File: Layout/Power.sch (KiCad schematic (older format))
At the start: 0 parts

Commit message: Add voltage regulators
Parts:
- added C? (x2): 10u, symbol Device:C
- added C?: 1u, symbol Device:C
- added C? (x4): 0.1u, symbol Device:C
- added C? (x2): 22u, symbol Device:C
- added D? (x4): US1M, Diode_SMD:D_SMA, symbol Diode:US1M
- added L?: 2.2u, symbol Device:L
- added R?: 49.9k, symbol Device:R_US
- added R?: 9.09k, symbol Device:R_US
- added R?: 1k, symbol Device:R_US
- added U?: TPS562200, Package_TO_SOT_SMD:SOT-23-6, symbol Regulator_Switching:TPS562200
- added U?: AP2112K-3.3, Package_TO_SOT_SMD:SOT-23-5, symbol Regulator_Linear:AP2112K-3.3
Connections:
- new net: C?.1, L?.1, U?.2 (SW)
- new net: R?.1, R?.1, U?.4 (VFB)
- new net: R?.1, U?.5 (EN)
- new net: C?.2, U?.6 (VBST)
- new net +3V3: C?.1, U?.5 (VOUT)
- new net +5V: C?.1, C?.1, C?.1, L?.2, R?.2, U?.1 (VIN), U?.3 (EN)
- new net +VDC: C?.1, C?.1, C?.1, C?.1, D?.1 (K), D?.1 (K), R?.2, U?.3 (VIN)
- new net GND: C?.2, C?.2, C?.2, C?.2, C?.2, C?.2, C?.2, C?.2, D?.2 (A), D?.2 (A), R?.2, U?.1 (GND), U?.2 (GND)
- new net PRI_HI: D?.1 (K), D?.2 (A)
- new net PRI_LO: D?.1 (K), D?.2 (A)

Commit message: Add footprints
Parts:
- C? (x9): footprint (none) -> Capacitor_SMD:C_0603_1608Metric_Pad1.05x0.95mm_HandSolder
- L?: footprint (none) -> Inductor_SMD:L_0603_1608Metric_Pad1.05x0.95mm_HandSolder
- R? (x3): footprint (none) -> Resistor_SMD:R_0603_1608Metric_Pad1.05x0.95mm_HandSolder
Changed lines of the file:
@@
 F 0 "C?" H 4465 2146 50  0000 L CNN
 F 1 "10u" H 4465 2055 50  0000 L CNN
-F 2 "" H 4388 1950 50  0001 C CNN
+F 2 "Capacitor_SMD:C_0603_1608Metric_Pad1.05x0.95mm_HandSolder" H 4388 1950 50  0001 C CNN
 F 3 "~" H 4350 2100 50  0001 C CNN
 	1    4350 2100
@@
 F 0 "C?" H 4865 2146 50  0000 L CNN
 F 1 "10u" H 4865 2055 50  0000 L CNN
-F 2 "" H 4788 1950 50  0001 C CNN
+F 2 "Capacitor_SMD:C_0603_1608Metric_Pad1.05x0.95mm_HandSolder" H 4788 1950 50  0001 C CNN
 F 3 "~" H 4750 2100 50  0001 C CNN
 	1    4750 2100
@@
 F 0 "C?" H 5265 2146 50  0000 L CNN
 F 1 "1u" H 5265 2055 50  0000 L CNN
-F 2 "" H 5188 1950 50  0001 C CNN
+F 2 "Capacitor_SMD:C_0603_1608Metric_Pad1.05x0.95mm_HandSolder" H 5188 1950 50  0001 C CNN
 F 3 "~" H 5150 2100 50  0001 C CNN
 	1    5150 2100
@@
 F 0 "C?" H 5665 2146 50  0000 L CNN
 F 1 "0.1u" H 5665 2055 50  0000 L CNN
-F 2 "" H 5588 1950 50  0001 C CNN
+F 2 "Capacitor_SMD:C_0603_1608Metric_Pad1.05x0.95mm_HandSolder" H 5588 1950 50  0001 C CNN
 F 3 "~" H 5550 2100 50  0001 C CNN
 	1    5550 2100
@@
 F 0 "L?" V 3790 4350 50  0000 C CNN
 F 1 "2.2u" V 3699 4350 50  0000 C CNN
-F 2 "" H 3600 4350 50  0001 C CNN
+F 2 "Inductor_SMD:L_0603_1608Metric_Pad1.05x0.95mm_HandSolder" H 3600 4350 50  0001 C CNN
 F 3 "~" H 3600 4350 50  0001 C CNN
 	1    3600 4350
@@
 F 0 "C?" V 3802 4900 50  0000 C CNN
 F 1 "0.1u" V 3711 4900 50  0000 C CNN
-F 2 "" H 3588 4750 50  0001 C CNN
+F 2 "Capacitor_SMD:C_0603_1608Metric_Pad1.05x0.95mm_HandSolder" H 3588 4750 50  0001 C CNN
 F 3 "~" H 3550 4900 50  0001 C CNN
 	1    3550 4900
@@
 F 0 "C?" H 4065 4546 50  0000 L CNN
 F 1 "22u" H 4065 4455 50  0000 L CNN
-F 2 "" H 3988 4350 50  0001 C CNN
+F 2 "Capacitor_SMD:C_0603_1608Metric_Pad1.05x0.95mm_HandSolder" H 3988 4350 50  0001 C CNN
 F 3 "~" H 3950 4500 50  0001 C CNN
 	1    3950 4500
@@
 F 0 "C?" H 4465 4546 50  0000 L CNN
 F 1 "22u" H 4465 4455 50  0000 L CNN
-F 2 "" H 4388 4350 50  0001 C CNN
+F 2 "Capacitor_SMD:C_0603_1608Metric_Pad1.05x0.95mm_HandSolder" H 4388 4350 50  0001 C CNN
 F 3 "~" H 4350 4500 50  0001 C CNN
 	1    4350 4500
@@
 F 0 "R?" V 4105 5100 50  0000 C CNN
 F 1 "49.9k" V 4014 5100 50  0000 C CNN
-F 2 "" V 3940 5090 50  0001 C CNN
+F 2 "Resistor_SMD:R_0603_1608Metric_Pad1.05x0.95mm_HandSolder" V 3940 5090 50  0001 C CNN
 F 3 "~" H 3900 5100 50  0001 C CNN
 	1    3900 5100
@@
 F 0 "R?" H 3418 5396 50  0000 L CNN
 F 1 "9.09k" H 3418 5305 50  0000 L CNN
-F 2 "" V 3390 5340 50  0001 C CNN
+F 2 "Resistor_SMD:R_0603_1608Metric_Pad1.05x0.95mm_HandSolder" V 3390 5340 50  0001 C CNN
 F 3 "~" H 3350 5350 50  0001 C CNN
 	1    3350 5350
@@
 F 0 "C?" H 6365 5396 50  0000 L CNN
 F 1 "0.1u" H 6365 5305 50  0000 L CNN
-F 2 "" H 6288 5200 50  0001 C CNN
+F 2 "Capacitor_SMD:C_0603_1608Metric_Pad1.05x0.95mm_HandSolder" H 6288 5200 50  0001 C CNN
 F 3 "~" H 6250 5350 50  0001 C CNN
 	1    6250 5350
@@
 F 0 "C?" H 7465 5396 50  0000 L CNN
 F 1 "0.1u" H 7465 5305 50  0000 L CNN
-F 2 "" H 7388 5200 50  0001 C CNN
+F 2 "Capacitor_SMD:C_0603_1608Metric_Pad1.05x0.95mm_HandSolder" H 7388 5200 50  0001 C CNN
 F 3 "~" H 7350 5350 50  0001 C CNN
 	1    7350 5350
@@
 F 0 "R?" V 2095 5100 50  0000 C CNN
 F 1 "1k" V 2186 5100 50  0000 C CNN
-F 2 "" V 2340 5090 50  0001 C CNN
+F 2 "Resistor_SMD:R_0603_1608Metric_Pad1.05x0.95mm_HandSolder" V 2340 5090 50  0001 C CNN
 F 3 "~" H 2300 5100 50  0001 C CNN
 	1    2300 5100

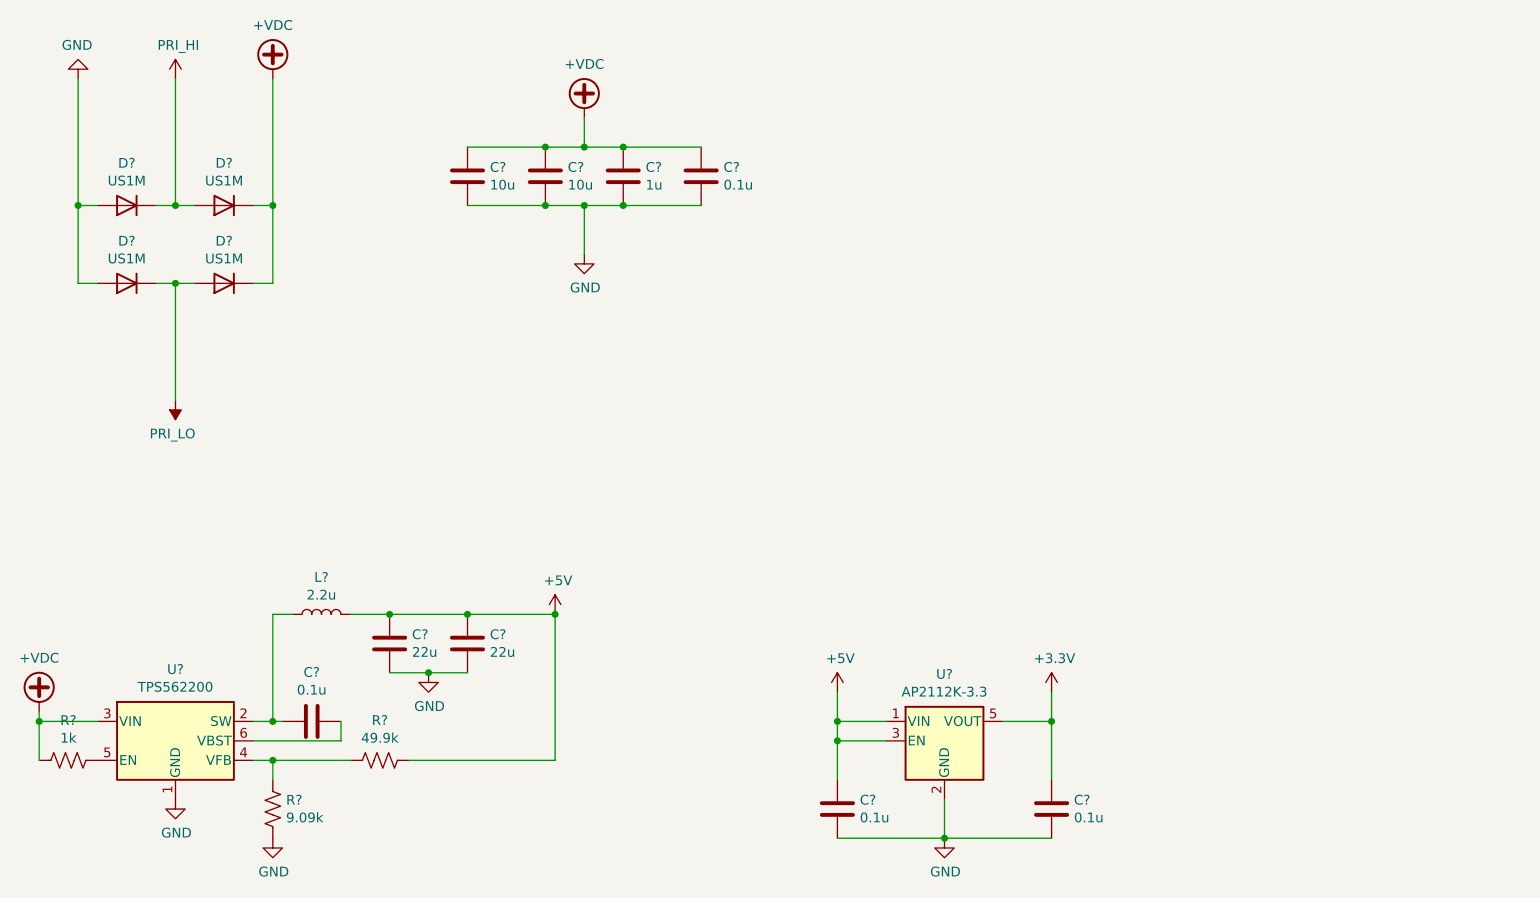
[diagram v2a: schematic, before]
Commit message: Update footprints and references
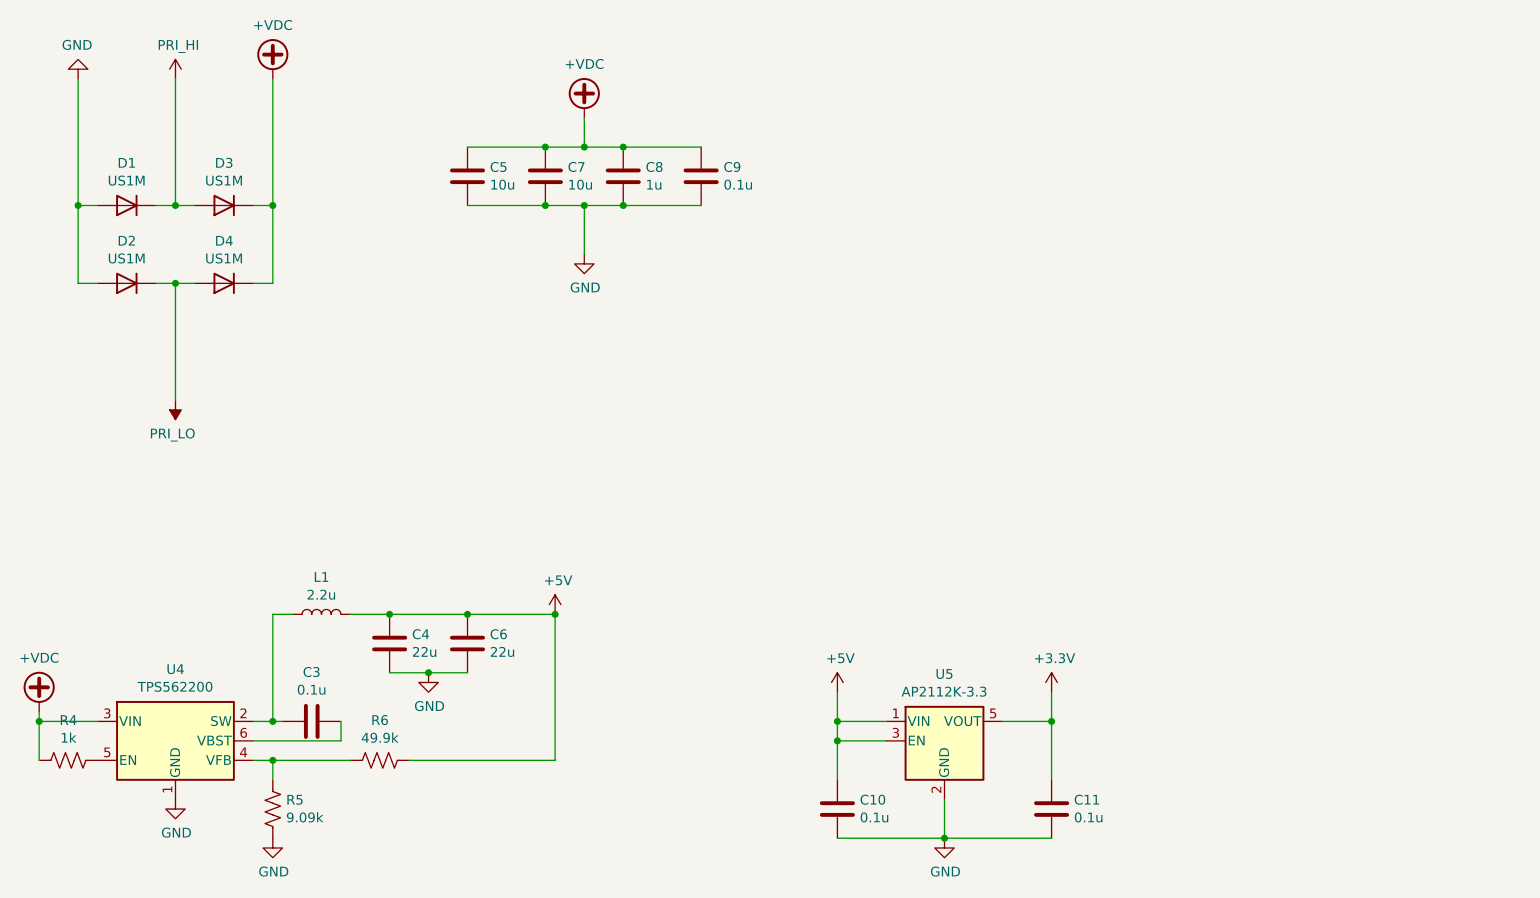
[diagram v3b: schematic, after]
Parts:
- gave numbers to parts that had none: 19
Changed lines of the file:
@@
 $EndDescr
 $Comp
-L Diode:US1M D?
+L Diode:US1M D1
 U 1 1 5F35FDF9
 P 2600 2250
-F 0 "D?" H 2600 2033 50  0000 C CNN
+F 0 "D1" H 2600 2033 50  0000 C CNN
 F 1 "US1M" H 2600 2124 50  0000 C CNN
 F 2 "Diode_SMD:D_SMA" H 2600 2075 50  0001 C CNN
@@
 $EndComp
 $Comp
-L Diode:US1M D?
+L Diode:US1M D3
 U 1 1 5F360A65
 P 3100 2250
-F 0 "D?" H 3100 2033 50  0000 C CNN
+F 0 "D3" H 3100 2033 50  0000 C CNN
 F 1 "US1M" H 3100 2124 50  0000 C CNN
 F 2 "Diode_SMD:D_SMA" H 3100 2075 50  0001 C CNN
@@
 $EndComp
 $Comp
-L Diode:US1M D?
+L Diode:US1M D2
 U 1 1 5F36109C
 P 2600 2650
-F 0 "D?" H 2600 2433 50  0000 C CNN
+F 0 "D2" H 2600 2433 50  0000 C CNN
 F 1 "US1M" H 2600 2524 50  0000 C CNN
 F 2 "Diode_SMD:D_SMA" H 2600 2475 50  0001 C CNN
@@
 $EndComp
 $Comp
-L Diode:US1M D?
+L Diode:US1M D4
 U 1 1 5F3616CE
 P 3100 2650
-F 0 "D?" H 3100 2433 50  0000 C CNN
+F 0 "D4" H 3100 2433 50  0000 C CNN
 F 1 "US1M" H 3100 2524 50  0000 C CNN
 F 2 "Diode_SMD:D_SMA" H 3100 2475 50  0001 C CNN
@@
 	2850 2650 2950 2650
 $Comp
-L power:GND #PWR?
+L power:GND #PWR0121
 U 1 1 5F36338B
 P 2350 1600
-F 0 "#PWR?" H 2350 1350 50  0001 C CNN
+F 0 "#PWR0121" H 2350 1350 50  0001 C CNN
 F 1 "GND" H 2355 1427 50  0000 C CNN
 F 2 "" H 2350 1600 50  0001 C CNN
@@
 $EndComp
 $Comp
-L power:PRI_HI #PWR?
+L power:PRI_HI #PWR0122
 U 1 1 5F363BA1
 P 2850 1600
-F 0 "#PWR?" H 2850 1450 50  0001 C CNN
+F 0 "#PWR0122" H 2850 1450 50  0001 C CNN
 F 1 "PRI_HI" H 2865 1773 50  0000 C CNN
 F 2 "" H 2850 1600 50  0001 C CNN
@@
 $EndComp
 $Comp
-L power:PRI_LO #PWR?
+L power:PRI_LO #PWR0123
 U 1 1 5F363FB3
 P 2850 3250
-F 0 "#PWR?" H 2850 3100 50  0001 C CNN
+F 0 "#PWR0123" H 2850 3100 50  0001 C CNN
 F 1 "PRI_LO" H 2865 3423 50  0000 C CNN
 F 2 "" H 2850 3250 50  0001 C CNN
@@
 $EndComp
 $Comp
-L power:+VDC #PWR?
+L power:+VDC #PWR0124
 U 1 1 5F364724
 P 3350 1600
-F 0 "#PWR?" H 3350 1500 50  0001 C CNN
+F 0 "#PWR0124" H 3350 1500 50  0001 C CNN
 F 1 "+VDC" H 3350 1875 50  0000 C CNN
 F 2 "" H 3350 1600 50  0001 C CNN
@@
 $EndComp
 $Comp
-L power:+VDC #PWR?
+L power:+VDC #PWR0125
 U 1 1 5F36782D
 P 4950 1800
-F 0 "#PWR?" H 4950 1700 50  0001 C CNN
+F 0 "#PWR0125" H 4950 1700 50  0001 C CNN
 F 1 "+VDC" H 4950 2075 50  0000 C CNN
 F 2 "" H 4950 1800 50  0001 C CNN
@@
 $EndComp
 $Comp
-L Device:C C?
+L Device:C C5
 U 1 1 5F368682
 P 4350 2100
-F 0 "C?" H 4465 2146 50  0000 L CNN
+F 0 "C5" H 4465 2146 50  0000 L CNN
 F 1 "10u" H 4465 2055 50  0000 L CNN
 F 2 "Capacitor_SMD:C_0603_1608Metric_Pad1.05x0.95mm_HandSolder" H 4388 1950 50  0001 C CNN
@@
 $EndComp
 $Comp
-L Device:C C?
+L Device:C C7
 U 1 1 5F368CA1
 P 4750 2100
-F 0 "C?" H 4865 2146 50  0000 L CNN
+F 0 "C7" H 4865 2146 50  0000 L CNN
 F 1 "10u" H 4865 2055 50  0000 L CNN
 F 2 "Capacitor_SMD:C_0603_1608Metric_Pad1.05x0.95mm_HandSolder" H 4788 1950 50  0001 C CNN
@@
 $EndComp
 $Comp
-L Device:C C?
+L Device:C C8
 U 1 1 5F368F24
 P 5150 2100
-F 0 "C?" H 5265 2146 50  0000 L CNN
+F 0 "C8" H 5265 2146 50  0000 L CNN
 F 1 "1u" H 5265 2055 50  0000 L CNN
 F 2 "Capacitor_SMD:C_0603_1608Metric_Pad1.05x0.95mm_HandSolder" H 5188 1950 50  0001 C CNN
@@
 $EndComp
 $Comp
-L Device:C C?
+L Device:C C9
 U 1 1 5F3693E0
 P 5550 2100
-F 0 "C?" H 5665 2146 50  0000 L CNN
+F 0 "C9" H 5665 2146 50  0000 L CNN
 F 1 "0.1u" H 5665 2055 50  0000 L CNN
 F 2 "Capacitor_SMD:C_0603_1608Metric_Pad1.05x0.95mm_HandSolder" H 5588 1950 50  0001 C CNN
@@
 	4950 1950 5150 1950
 $Comp
-L power:GND #PWR?
+L power:GND #PWR0126
 U 1 1 5F36AFC7
 P 4950 2500
-F 0 "#PWR?" H 4950 2250 50  0001 C CNN
+F 0 "#PWR0126" H 4950 2250 50  0001 C CNN
 F 1 "GND" H 4955 2327 50  0000 C CNN
 F 2 "" H 4950 2500 50  0001 C CNN
@@
 	4950 2250 5150 2250
 $Comp
-L Regulator_Switching:TPS562200 U?
+L Regulator_Switching:TPS562200 U4
 U 1 1 5F37D6F5
 P 2850 5000
-F 0 "U?" H 2850 5367 50  0000 C CNN
+F 0 "U4" H 2850 5367 50  0000 C CNN
 F 1 "TPS562200" H 2850 5276 50  0000 C CNN
 F 2 "Package_TO_SOT_SMD:SOT-23-6" H 2900 4750 50  0001 L CNN
@@
 $EndComp
 $Comp
-L power:+VDC #PWR?
+L power:+VDC #PWR0127
 U 1 1 5F37D6FB
 P 2150 4850
-F 0 "#PWR?" H 2150 4750 50  0001 C CNN
+F 0 "#PWR0127" H 2150 4750 50  0001 C CNN
 F 1 "+VDC" H 2150 5125 50  0000 C CNN
 F 2 "" H 2150 4850 50  0001 C CNN
@@
 	2150 4900 2450 4900
 $Comp
-L Device:L L?
+L Device:L L1
 U 1 1 5F37D703
 P 3600 4350
-F 0 "L?" V 3790 4350 50  0000 C CNN
+F 0 "L1" V 3790 4350 50  0000 C CNN
 F 1 "2.2u" V 3699 4350 50  0000 C CNN
 F 2 "Inductor_SMD:L_0603_1608Metric_Pad1.05x0.95mm_HandSolder" H 3600 4350 50  0001 C CNN
@@
 $EndComp
 $Comp
-L Device:C C?
+L Device:C C3
 U 1 1 5F37D709
 P 3550 4900
-F 0 "C?" V 3802 4900 50  0000 C CNN
+F 0 "C3" V 3802 4900 50  0000 C CNN
 F 1 "0.1u" V 3711 4900 50  0000 C CNN
 F 2 "Capacitor_SMD:C_0603_1608Metric_Pad1.05x0.95mm_HandSolder" H 3588 4750 50  0001 C CNN
@@
 	3350 4350 3450 4350
 $Comp
-L Device:C C?
+L Device:C C4
 U 1 1 5F37D716
 P 3950 4500
-F 0 "C?" H 4065 4546 50  0000 L CNN
+F 0 "C4" H 4065 4546 50  0000 L CNN
 F 1 "22u" H 4065 4455 50  0000 L CNN
 F 2 "Capacitor_SMD:C_0603_1608Metric_Pad1.05x0.95mm_HandSolder" H 3988 4350 50  0001 C CNN
@@
 $EndComp
 $Comp
-L Device:C C?
+L Device:C C6
 U 1 1 5F37D71C
 P 4350 4500
-F 0 "C?" H 4465 4546 50  0000 L CNN
+F 0 "C6" H 4465 4546 50  0000 L CNN
 F 1 "22u" H 4465 4455 50  0000 L CNN
 F 2 "Capacitor_SMD:C_0603_1608Metric_Pad1.05x0.95mm_HandSolder" H 4388 4350 50  0001 C CNN
@@
 Connection ~ 4350 4350
 $Comp
-L power:GND #PWR?
+L power:GND #PWR0128
 U 1 1 5F37D72E
 P 2850 5300
-F 0 "#PWR?" H 2850 5050 50  0001 C CNN
+F 0 "#PWR0128" H 2850 5050 50  0001 C CNN
 F 1 "GND" H 2855 5127 50  0000 C CNN
 F 2 "" H 2850 5300 50  0001 C CNN
@@
 $EndComp
 $Comp
-L power:GND #PWR?
+L power:GND #PWR0129
 U 1 1 5F37D734
 P 4150 4650
-F 0 "#PWR?" H 4150 4400 50  0001 C CNN
+F 0 "#PWR0129" H 4150 4400 50  0001 C CNN
 F 1 "GND" H 4155 4477 50  0000 C CNN
 F 2 "" H 4150 4650 50  0001 C CNN
@@
 	4150 4650 4350 4650
 $Comp
-L Device:R_US R?
+L Device:R_US R6
 U 1 1 5F37D73C
 P 3900 5100
-F 0 "R?" V 4105 5100 50  0000 C CNN
+F 0 "R6" V 4105 5100 50  0000 C CNN
 F 1 "49.9k" V 4014 5100 50  0000 C CNN
 F 2 "Resistor_SMD:R_0603_1608Metric_Pad1.05x0.95mm_HandSolder" V 3940 5090 50  0001 C CNN
@@
 	3750 5100 3350 5100
 $Comp
-L Device:R_US R?
+L Device:R_US R5
 U 1 1 5F37D743
 P 3350 5350
-F 0 "R?" H 3418 5396 50  0000 L CNN
+F 0 "R5" H 3418 5396 50  0000 L CNN
 F 1 "9.09k" H 3418 5305 50  0000 L CNN
 F 2 "Resistor_SMD:R_0603_1608Metric_Pad1.05x0.95mm_HandSolder" V 3390 5340 50  0001 C CNN
@@
 	3350 5100 3250 5100
 $Comp
-L power:GND #PWR?
+L power:GND #PWR0130
 U 1 1 5F37D74C
 P 3350 5500
-F 0 "#PWR?" H 3350 5250 50  0001 C CNN
+F 0 "#PWR0130" H 3350 5250 50  0001 C CNN
 F 1 "GND" H 3355 5327 50  0000 C CNN
 F 2 "" H 3350 5500 50  0001 C CNN
@@
 	4800 5100 4050 5100
 $Comp
-L power:+5V #PWR?
+L power:+5V #PWR0131
 U 1 1 5F37ED31
 P 4800 4350
-F 0 "#PWR?" H 4800 4200 50  0001 C CNN
+F 0 "#PWR0131" H 4800 4200 50  0001 C CNN
 F 1 "+5V" H 4815 4523 50  0000 C CNN
 F 2 "" H 4800 4350 50  0001 C CNN
@@
 Connection ~ 4800 4350
 $Comp
-L Regulator_Linear:AP2112K-3.3 U?
+L Regulator_Linear:AP2112K-3.3 U5
 U 1 1 5F388344
 P 6800 5000
-F 0 "U?" H 6800 5342 50  0000 C CNN
+F 0 "U5" H 6800 5342 50  0000 C CNN
 F 1 "AP2112K-3.3" H 6800 5251 50  0000 C CNN
 F 2 "Package_TO_SOT_SMD:SOT-23-5" H 6800 5325 50  0001 C CNN
@@
 $EndComp
 $Comp
-L Device:C C?
+L Device:C C10
 U 1 1 5F38A05E
 P 6250 5350
-F 0 "C?" H 6365 5396 50  0000 L CNN
+F 0 "C10" H 6365 5396 50  0000 L CNN
 F 1 "0.1u" H 6365 5305 50  0000 L CNN
 F 2 "Capacitor_SMD:C_0603_1608Metric_Pad1.05x0.95mm_HandSolder" H 6288 5200 50  0001 C CNN
@@
 $EndComp
 $Comp
-L Device:C C?
+L Device:C C11
 U 1 1 5F38A758
 P 7350 5350
-F 0 "C?" H 7465 5396 50  0000 L CNN
+F 0 "C11" H 7465 5396 50  0000 L CNN
 F 1 "0.1u" H 7465 5305 50  0000 L CNN
 F 2 "Capacitor_SMD:C_0603_1608Metric_Pad1.05x0.95mm_HandSolder" H 7388 5200 50  0001 C CNN
@@
 	6250 5000 6250 5200
 $Comp
-L power:GND #PWR?
+L power:GND #PWR0132
 U 1 1 5F38E9E5
 P 6800 5500
-F 0 "#PWR?" H 6800 5250 50  0001 C CNN
+F 0 "#PWR0132" H 6800 5250 50  0001 C CNN
 F 1 "GND" H 6805 5327 50  0000 C CNN
 F 2 "" H 6800 5500 50  0001 C CNN
@@
 $EndComp
 $Comp
-L power:+5V #PWR?
+L power:+5V #PWR0133
 U 1 1 5F38ECB3
 P 6250 4750
-F 0 "#PWR?" H 6250 4600 50  0001 C CNN
+F 0 "#PWR0133" H 6250 4600 50  0001 C CNN
 F 1 "+5V" H 6265 4923 50  0000 C CNN
 F 2 "" H 6250 4750 50  0001 C CNN
@@
 Connection ~ 6250 4900
 $Comp
-L power:+3.3V #PWR?
+L power:+3.3V #PWR0134
 U 1 1 5F38FD10
 P 7350 4750
-F 0 "#PWR?" H 7350 4600 50  0001 C CNN
+F 0 "#PWR0134" H 7350 4600 50  0001 C CNN
 F 1 "+3.3V" H 7365 4923 50  0000 C CNN
 F 2 "" H 7350 4750 50  0001 C CNN
@@
 Connection ~ 7350 4900
 $Comp
-L Device:R_US R?
+L Device:R_US R4
 U 1 1 5F393064
 P 2300 5100
-F 0 "R?" V 2095 5100 50  0000 C CNN
+F 0 "R4" V 2095 5100 50  0000 C CNN
 F 1 "1k" V 2186 5100 50  0000 C CNN
 F 2 "Resistor_SMD:R_0603_1608Metric_Pad1.05x0.95mm_HandSolder" V 2340 5090 50  0001 C CNN

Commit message: Layout
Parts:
- L1: footprint Inductor_SMD:L_0603_1608Metric_Pad1.05x0.95mm_HandSolder -> Inductor_SMD:L_Taiyo-Yuden_NR-40xx_HandSoldering
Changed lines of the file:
@@
 F 0 "L1" V 3790 4350 50  0000 C CNN
 F 1 "2.2u" V 3699 4350 50  0000 C CNN
-F 2 "Inductor_SMD:L_0603_1608Metric_Pad1.05x0.95mm_HandSolder" H 3600 4350 50  0001 C CNN
+F 2 "Inductor_SMD:L_Taiyo-Yuden_NR-40xx_HandSoldering" H 3600 4350 50  0001 C CNN
 F 3 "~" H 3600 4350 50  0001 C CNN
 	1    3600 4350
